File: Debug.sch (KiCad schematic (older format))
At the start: 3 parts, among them J8 Conn_ARM_JTAG_SWD_10

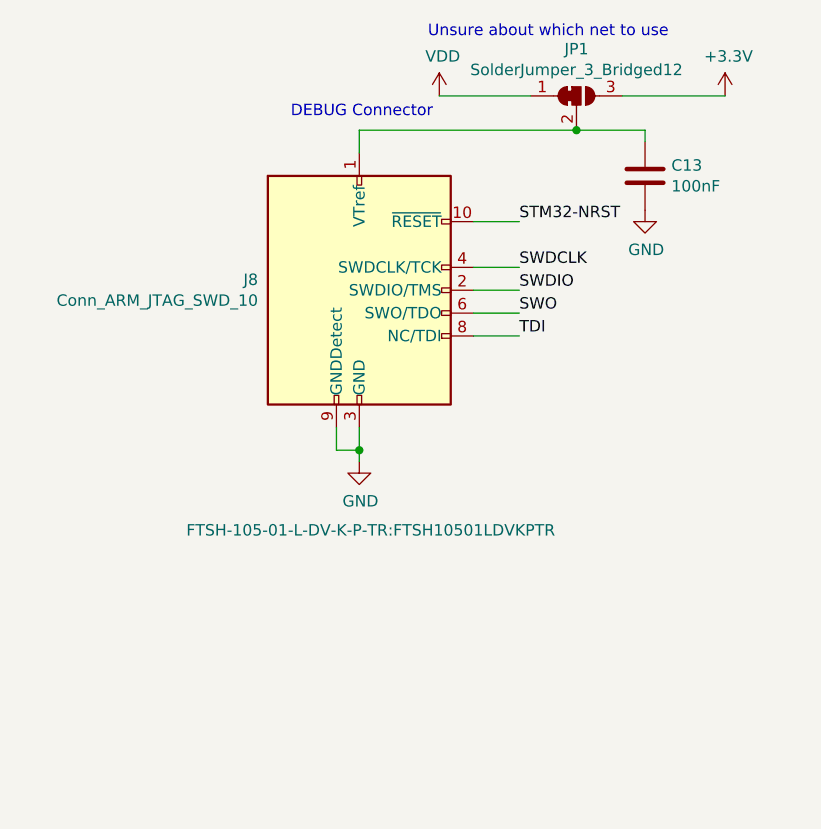
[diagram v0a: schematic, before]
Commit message: Added in Debug sheet
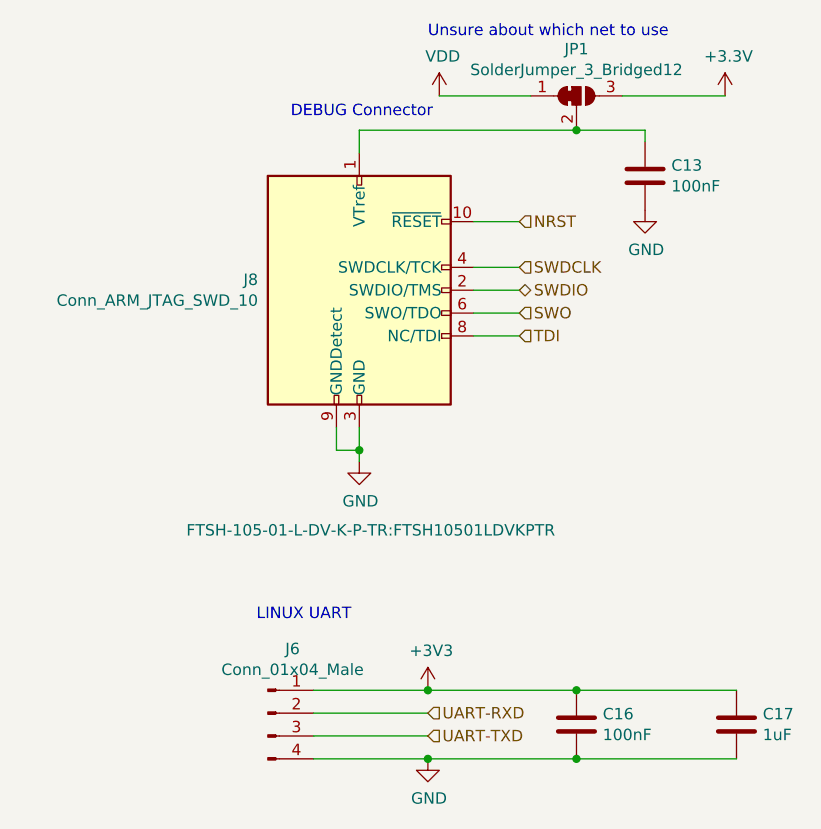
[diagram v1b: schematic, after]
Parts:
- added C16: 100nF, symbol Device:C
- added C17: 1uF, symbol Device:C
- added J6: Conn_01x04_Male, symbol Connector:Conn_01x04_Male
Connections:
- net +3V3: now also C16.1, C17.1, J6.1 (Pin_1)
- net GND: now also C16.2, C17.2, J6.4 (Pin_4)
- net STM32-NRST renamed NRST
- new net UART-RXD: J6.2 (Pin_2)
- new net UART-TXD: J6.3 (Pin_3)
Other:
- note added: "LINUX UART"
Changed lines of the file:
@@
 $Descr A4 11693 8268
 encoding utf-8
-Sheet 3 3
-Title ""
+Sheet 2 3
+Title "Contains Debugging connectors for Rev1"
 Date "1"
 Rev "1"
@@
 Wire Wire Line
 	2800 3100 3000 3100
-Text Label 3000 3100 0    50   ~ 0
-STM32-NRST
 Wire Wire Line
 	2800 3300 3000 3300
 Wire Wire Line
 	2800 3400 3000 3400
-Text Label 3000 3400 0    50   ~ 0
-SWDIO
 Wire Wire Line
 	2800 3500 3000 3500
-Text Label 3000 3300 0    50   ~ 0
-SWDCLK
-Text Label 3000 3500 0    50   ~ 0
-SWO
 Wire Wire Line
 	2800 3600 3000 3600
-Text Label 3000 3600 0    50   ~ 0
-TDI
 $Comp
 L power:GND #PWR?
@@
 Text Notes 2600 2300 0    50   ~ 0
 Unsure about which net to use\n
+$Comp
+L power:+3V3 #PWR?
+U 1 1 5EEEFC78
+P 2600 5150
+AR Path="/5EEEFC78" Ref="#PWR?"  Part="1"
+AR Path="/5EDB4AB1/5EEEFC78" Ref="#PWR01"  Part="1"
+F 0 "#PWR01" H 2600 5000 50  0001 C CNN
+F 1 "+3V3" H 2615 5323 50  0000 C CNN
+F 2 "" H 2600 5150 50  0001 C CNN
+F 3 "" H 2600 5150 50  0001 C CNN
+	1    2600 5150
+	1    0    0    -1
+$EndComp
+$Comp
+L power:GND #PWR?
+U 1 1 5EEEFC7E
+P 2600 5450
+AR Path="/5EEEFC7E" Ref="#PWR?"  Part="1"
+AR Path="/5EDB4AB1/5EEEFC7E" Ref="#PWR02"  Part="1"
+F 0 "#PWR02" H 2600 5200 50  0001 C CNN
+F 1 "GND" H 2605 5277 50  0000 C CNN
+F 2 "" H 2600 5450 50  0001 C CNN
+F 3 "" H 2600 5450 50  0001 C CNN
+	1    2600 5450
+	1    0    0    -1
+$EndComp
+Wire Wire Line
+	2100 5450 2600 5450
+Wire Wire Line
+	2100 5350 2600 5350
+Wire Wire Line
+	2100 5250 2600 5250
+Wire Wire Line
+	2100 5150 2600 5150
+Text Notes 1850 4850 0    50   ~ 0
+LINUX UART
+$Comp
+L Connector:Conn_01x04_Male J?
+U 1 1 5EEEFC89
+P 1900 5250
+AR Path="/5EEEFC89" Ref="J?"  Part="1"
+AR Path="/5EDB4AB1/5EEEFC89" Ref="J6"  Part="1"
+F 0 "J6" H 2008 5531 50  0000 C CNN
+F 1 "Conn_01x04_Male" H 2008 5440 50  0000 C CNN
+F 2 "" H 1900 5250 50  0001 C CNN
+F 3 "~" H 1900 5250 50  0001 C CNN
+	1    1900 5250
+	1    0    0    -1
+$EndComp
+Text HLabel 3000 3300 2    50   Input ~ 0
+SWDCLK
+Text HLabel 3000 3400 2    50   BiDi ~ 0
+SWDIO
+Text HLabel 3000 3500 2    50   Input ~ 0
+SWO
+Text HLabel 3000 3600 2    50   Input ~ 0
+TDI
+Text HLabel 3000 3100 2    50   Input ~ 0
+NRST
+Text HLabel 2600 5250 2    50   Input ~ 0
+UART-RXD
+Text HLabel 2600 5350 2    50   Input ~ 0
+UART-TXD
+$Comp
+L Device:C C16
+U 1 1 5EEF13AB
+P 3250 5300
+F 0 "C16" H 3365 5346 50  0000 L CNN
+F 1 "100nF" H 3365 5255 50  0000 L CNN
+F 2 "" H 3288 5150 50  0001 C CNN
+F 3 "~" H 3250 5300 50  0001 C CNN
+	1    3250 5300
+	1    0    0    -1
+$EndComp
+Wire Wire Line
+	2600 5150 3250 5150
+Connection ~ 2600 5150
+Wire Wire Line
+	3250 5450 2600 5450
+Connection ~ 2600 5450
+$Comp
+L Device:C C17
+U 1 1 5EEF31BC
+P 3950 5300
+F 0 "C17" H 4065 5346 50  0000 L CNN
+F 1 "1uF" H 4065 5255 50  0000 L CNN
+F 2 "" H 3988 5150 50  0001 C CNN
+F 3 "~" H 3950 5300 50  0001 C CNN
+	1    3950 5300
+	1    0    0    -1
+$EndComp
+Wire Wire Line
+	3250 5150 3950 5150
+Connection ~ 3250 5150
+Wire Wire Line
+	3950 5450 3250 5450
+Connection ~ 3250 5450
 $EndSCHEMATC

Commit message: Wired up IMUs signals
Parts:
- C16: footprint (none) -> Capacitor_SMD:C_0603_1608Metric_Pad1.05x0.95mm_HandSolder
- C17: Part No (none) -> TMK107BLD105MA-T
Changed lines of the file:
@@
 F 0 "C16" H 3365 5346 50  0000 L CNN
 F 1 "100nF" H 3365 5255 50  0000 L CNN
-F 2 "" H 3288 5150 50  0001 C CNN
+F 2 "Capacitor_SMD:C_0603_1608Metric_Pad1.05x0.95mm_HandSolder" H 3288 5150 50  0001 C CNN
 F 3 "~" H 3250 5300 50  0001 C CNN
 	1    3250 5300
@@
 F 2 "" H 3988 5150 50  0001 C CNN
 F 3 "~" H 3950 5300 50  0001 C CNN
+F 4 "TMK107BLD105MA-T" H 3950 5300 50  0001 C CNN "Part No"
 	1    3950 5300
 	1    0    0    -1
